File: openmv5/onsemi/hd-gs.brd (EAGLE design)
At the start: 35.6 x 16.5 mm, 60 parts, among them IC1 TLV62568PDDCR, IC2 AR0144CSSC20SUKA0, IC3 MIC5365-2.8YC5-TR, J1 DF12-36-DP, Q1 PMXB120EPEZ

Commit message: Finish out new onsemi cameras
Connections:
- removed net DCMI_D12: J1.8
- removed net DCMI_D13: J1.6
- net GND: now also J1.6, J1.8
- net SPI_MISO: now also IC2.P$48
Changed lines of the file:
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@@
 <contactref element="IC2" pad="P$8"/>
 <contactref element="IC2" pad="P$15"/>
+<contactref element="J1" pad="6"/>
+<contactref element="J1" pad="8"/>
 <wire x1="23.106" y1="9.9695" x2="23.9505" y2="11.43" width="0" layer="19" extent="1-1"/>
 <wire x1="21.5265" y1="8.6915" x2="23.106" y2="9.9695" width="0" layer="19" extent="1-1"/>
@@
 <wire x1="13.97" y1="8.1995" x2="15.438" y2="7.436" width="0" layer="19" extent="1-1"/>
 <wire x1="19.431" y1="13.981" x2="17.9705" y2="13.1365" width="0" layer="19" extent="1-1"/>
+<wire x1="20.53" y1="14.5001" x2="19.431" y2="13.981" width="0" layer="19" extent="1-16"/>
+<wire x1="21.03" y1="14.5001" x2="20.53" y2="14.5001" width="0" layer="19" extent="16-16"/>
 <wire x1="12.446" y1="7.355" x2="13.97" y2="8.1995" width="0" layer="19" extent="1-1"/>
 <wire x1="16.129" y1="3.691" x2="16.002" y2="5.592" width="0" layer="19" extent="1-16"/>
@@
 <signal name="SPI_MISO" class="4">
 <contactref element="J1" pad="15"/>
+<contactref element="IC2" pad="P$48"/>
+<wire x1="18.288" y1="7.436" x2="18.53" y2="10.8999" width="0" layer="19" extent="1-16"/>
 </signal>
 <signal name="SPI_MOSI" class="4">
@@
 <wire x1="17.148" y1="8.756" x2="16.53" y2="14.5001" width="0" layer="19" extent="1-16"/>
 </signal>
-<signal name="DCMI_D13" class="4">
-<contactref element="J1" pad="6"/>
-</signal>
-<signal name="DCMI_D12" class="4">
-<contactref element="J1" pad="8"/>
-</signal>
 <signal name="SW" class="3">

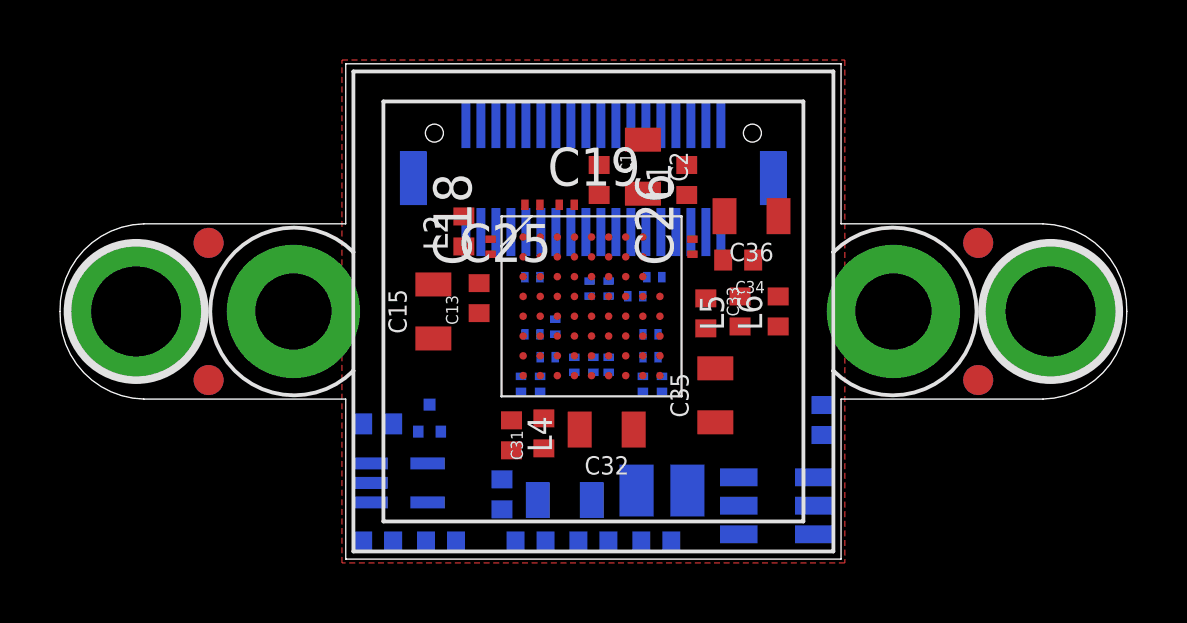
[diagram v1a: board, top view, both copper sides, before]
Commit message: Update camera modules to use different non-flippable pmosfet
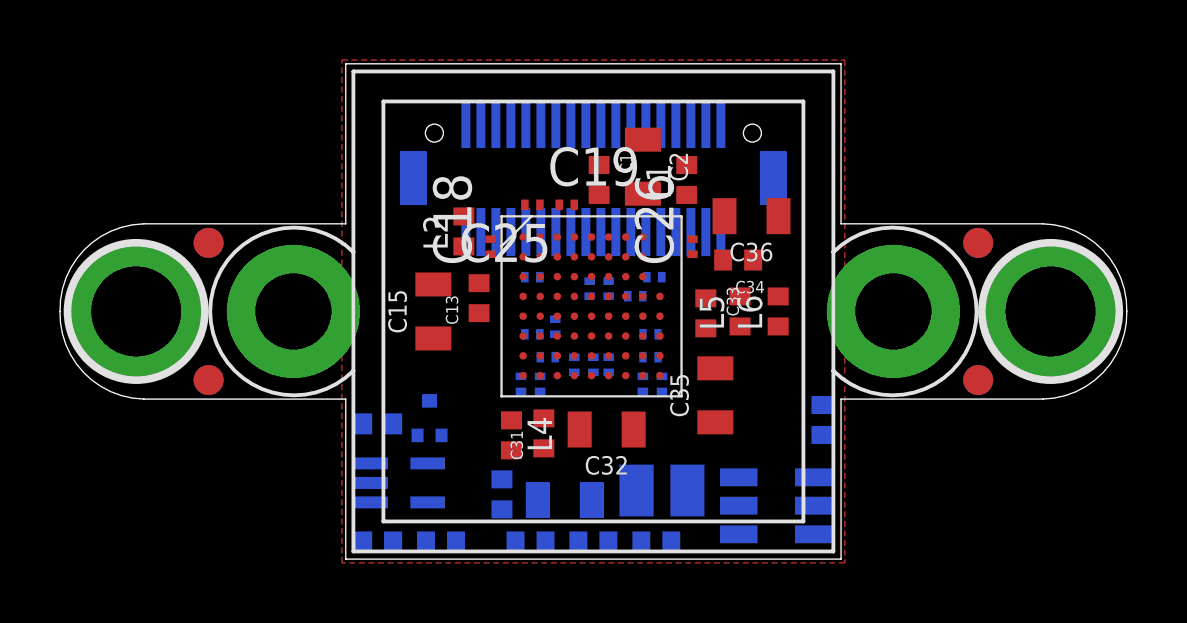
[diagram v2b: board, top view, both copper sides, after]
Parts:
- Q1: value PMXB120EPEZ -> SSM3J15FV,L3F; device PMXB120EPEZ:PMXB120EPEZ -> SSM3J15FV_L3F:SSM3J15FVL3F
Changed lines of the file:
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@@
 <attribute name="VALUE" x="18.542" y="13.081" size="0.6096" layer="27" font="vector" ratio="20" rot="R270" align="top-center"/>
 </element>
-<element name="Q1" library="PMXB120EPEZ" package="PMXB120EPEZ" value="PMXB120EPEZ" x="12.319" y="4.699" smashed="yes" rot="MR0">
-<attribute name="DESCRIPTION" value="MOSFET 30 V, P-channel Trench MOSFET" x="15.367" y="4.699" size="1.778" layer="28" rot="MR0" display="off"/>
-<attribute name="HEIGHT" value="0.4mm" x="15.367" y="4.699" size="1.778" layer="28" rot="MR0" display="off"/>
-<attribute name="MANUFACTURER_NAME" value="Nexperia" x="15.367" y="4.699" size="1.778" layer="28" rot="MR0" display="off"/>
-<attribute name="MANUFACTURER_PART_NUMBER" value="PMXB120EPEZ" x="15.367" y="4.699" size="1.778" layer="28" rot="MR0" display="off"/>
-<attribute name="MOUSER_PART_NUMBER" value="771-PMXB120EPEZ" x="15.367" y="4.699" size="1.778" layer="28" rot="MR0" display="off"/>
-<attribute name="MOUSER_PRICE-STOCK" value="https://www.mouser.co.uk/ProductDetail/Nexperia/PMXB120EPEZ?qs=gNSudQoqUYCYLaOobF3dPA%3D%3D" x="15.367" y="4.699" size="1.778" layer="28" rot="MR0" display="off"/>
-<attribute name="MPN" value="PMXB120EPEZ" x="15.367" y="4.699" size="1.778" layer="28" rot="MR0" display="off"/>
+<element name="Q1" library="SSM3J15FV_L3F" package="SSM3J15FVL3F" value="SSM3J15FV,L3F" x="12.319" y="4.699" smashed="yes" rot="MR0">
+<attribute name="DESCRIPTION" value="MOSFET Small-signal MOSFET High Speed Switching" x="15.367" y="4.699" size="1.778" layer="28" rot="MR0" display="off"/>
+<attribute name="HEIGHT" value="0.55mm" x="15.367" y="4.699" size="1.778" layer="28" rot="MR0" display="off"/>
+<attribute name="MANUFACTURER_NAME" value="Toshiba" x="15.367" y="4.699" size="1.778" layer="28" rot="MR0" display="off"/>
+<attribute name="MANUFACTURER_PART_NUMBER" value="SSM3J15FV,L3F" x="15.367" y="4.699" size="1.778" layer="28" rot="MR0" display="off"/>
+<attribute name="MOUSER_PART_NUMBER" value="757-SSM3J15FVL3F" x="15.367" y="4.699" size="1.778" layer="28" rot="MR0" display="off"/>
+<attribute name="MOUSER_PRICE-STOCK" value="https://www.mouser.co.uk/ProductDetail/Toshiba/SSM3J15FVL3F?qs=PDgMCp4xDJb4qTgE7FAUzA%3D%3D" x="15.367" y="4.699" size="1.778" layer="28" rot="MR0" display="off"/>
+<attribute name="MPN" value="SSM3J15FV,L3F" x="15.367" y="4.699" size="1.778" layer="28" rot="MR0" display="off"/>
 <attribute name="NAME" x="12.319" y="4.699" size="1.27" layer="26" rot="MR0" align="center"/>
 <attribute name="VALUE" x="12.319" y="4.699" size="1.27" layer="28" rot="MR0" align="center"/>
@@
 <contactref element="C30" pad="2"/>
 <contactref element="Q1" pad="2"/>
-<wire x1="10.1045" y1="0.5715" x2="10.353" y2="1.89" width="0" layer="19" extent="1-16"/>
-<wire x1="11.944" y1="4.249" x2="10.353" y2="1.89" width="0" layer="19" extent="16-16"/>
-<wire x1="21.53" y1="14.5001" x2="11.944" y2="4.249" width="0" layer="19" extent="16-16"/>
+<wire x1="11.919" y1="4.124" x2="21.53" y2="14.5001" width="0" layer="19" extent="16-16"/>
+<wire x1="10.353" y1="1.89" x2="11.919" y2="4.124" width="0" layer="19" extent="16-16"/>
+<wire x1="10.1045" y1="0.5715" x2="10.353" y2="1.89" width="0" layer="19" extent="16-16"/>
 </signal>
 <signal name="VCC" class="3">
@@
 <contactref element="J1" pad="25"/>
 <contactref element="Q1" pad="1"/>
-<wire x1="16.03" y1="10.8999" x2="12.694" y2="4.249" width="0" layer="19" extent="1-16"/>
+<wire x1="12.719" y1="4.124" x2="16.03" y2="10.8999" width="0" layer="19" extent="16-16"/>
 </signal>
 <signal name="DCMI_D4" class="4">
@@
 <contactref element="R4" pad="1"/>
 <contactref element="Q1" pad="3"/>
-<wire x1="11.1045" y1="4.5085" x2="10.353" y2="3.19" width="0" layer="19" extent="16-16"/>
-<wire x1="12.319" y1="5.149" x2="11.1045" y2="4.5085" width="0" layer="19" extent="16-16"/>
+<wire x1="11.1045" y1="4.5085" x2="12.319" y2="5.274" width="0" layer="19" extent="16-16"/>
+<wire x1="10.353" y1="3.19" x2="11.1045" y2="4.5085" width="0" layer="19" extent="16-16"/>
 </signal>
 <signal name="RESET_N" class="4">
